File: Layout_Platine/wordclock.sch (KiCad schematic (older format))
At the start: 71 parts, among them IC1 ATmega8, P1 DCF_CONN_4, P10 CONN_1, P13 P_led, P14 CONN_2, P2 5V_CONN_2, P3 ISP, P4 UART_CONN_6, P5 Led_Zeilen_CONN_11, P6 Led_Spalten_CONN_11, P7 CONN_1, P8 CONN_1, P9 CONN_1, Q1 BC817, Q2 BC807, U1 LM317, U3 74HC04, X1 10MHz

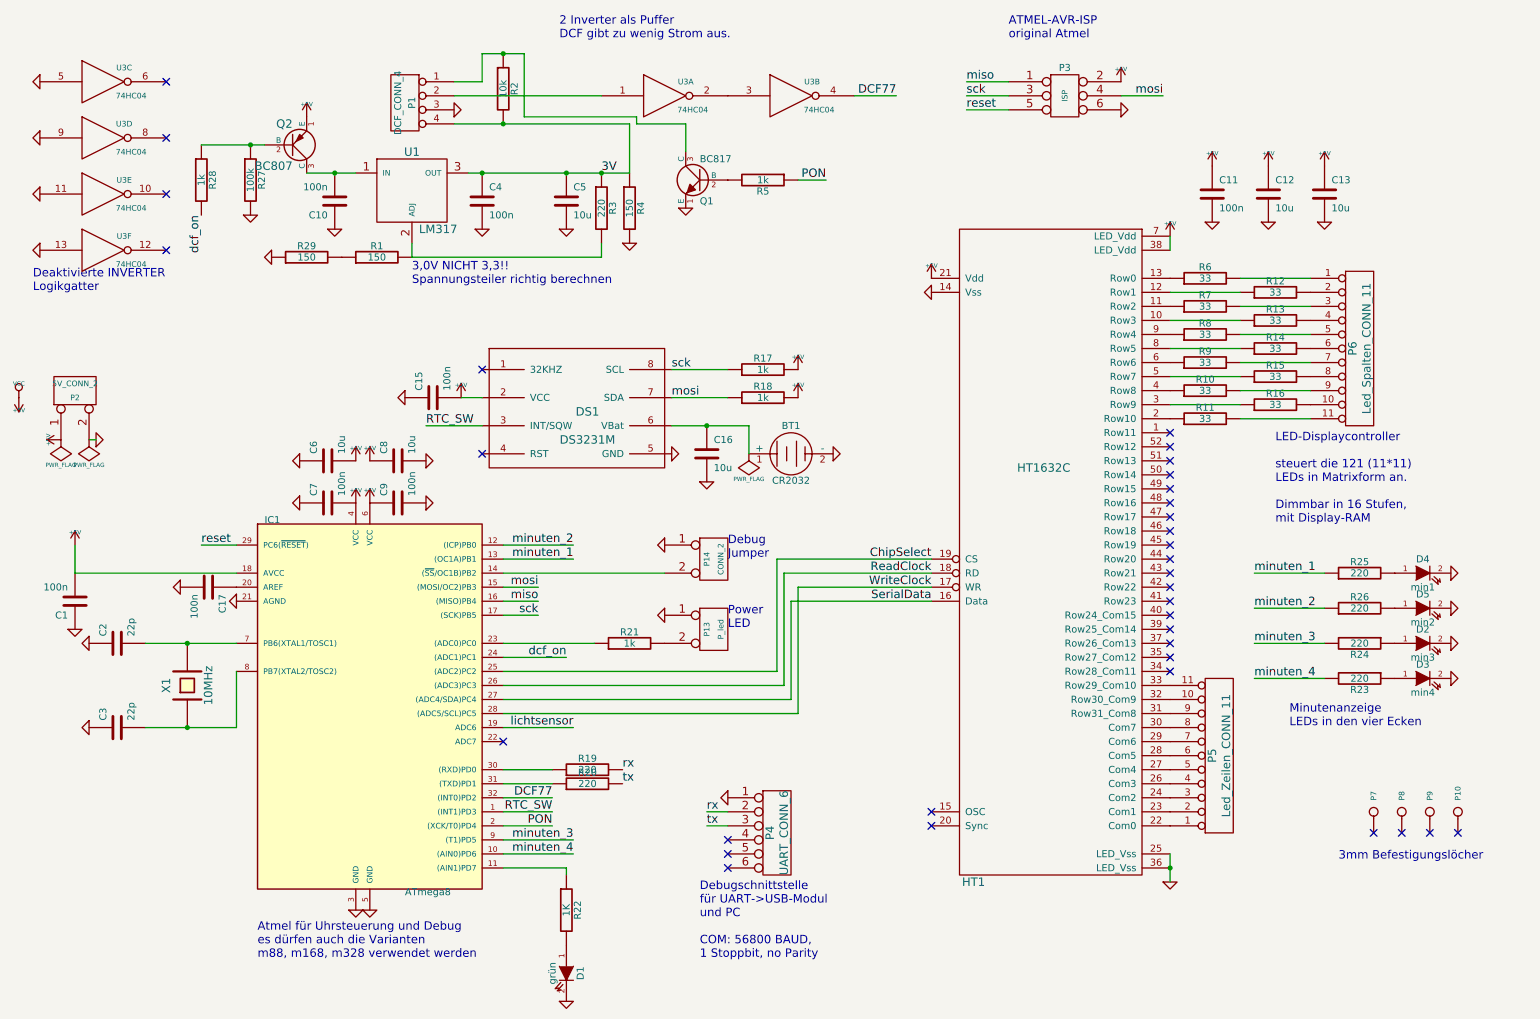
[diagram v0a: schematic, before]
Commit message: HardwareVersion 5 an sich fertig zur Herstellung. nur noch kleinere Änderungen, keine weiteren Features mehr.
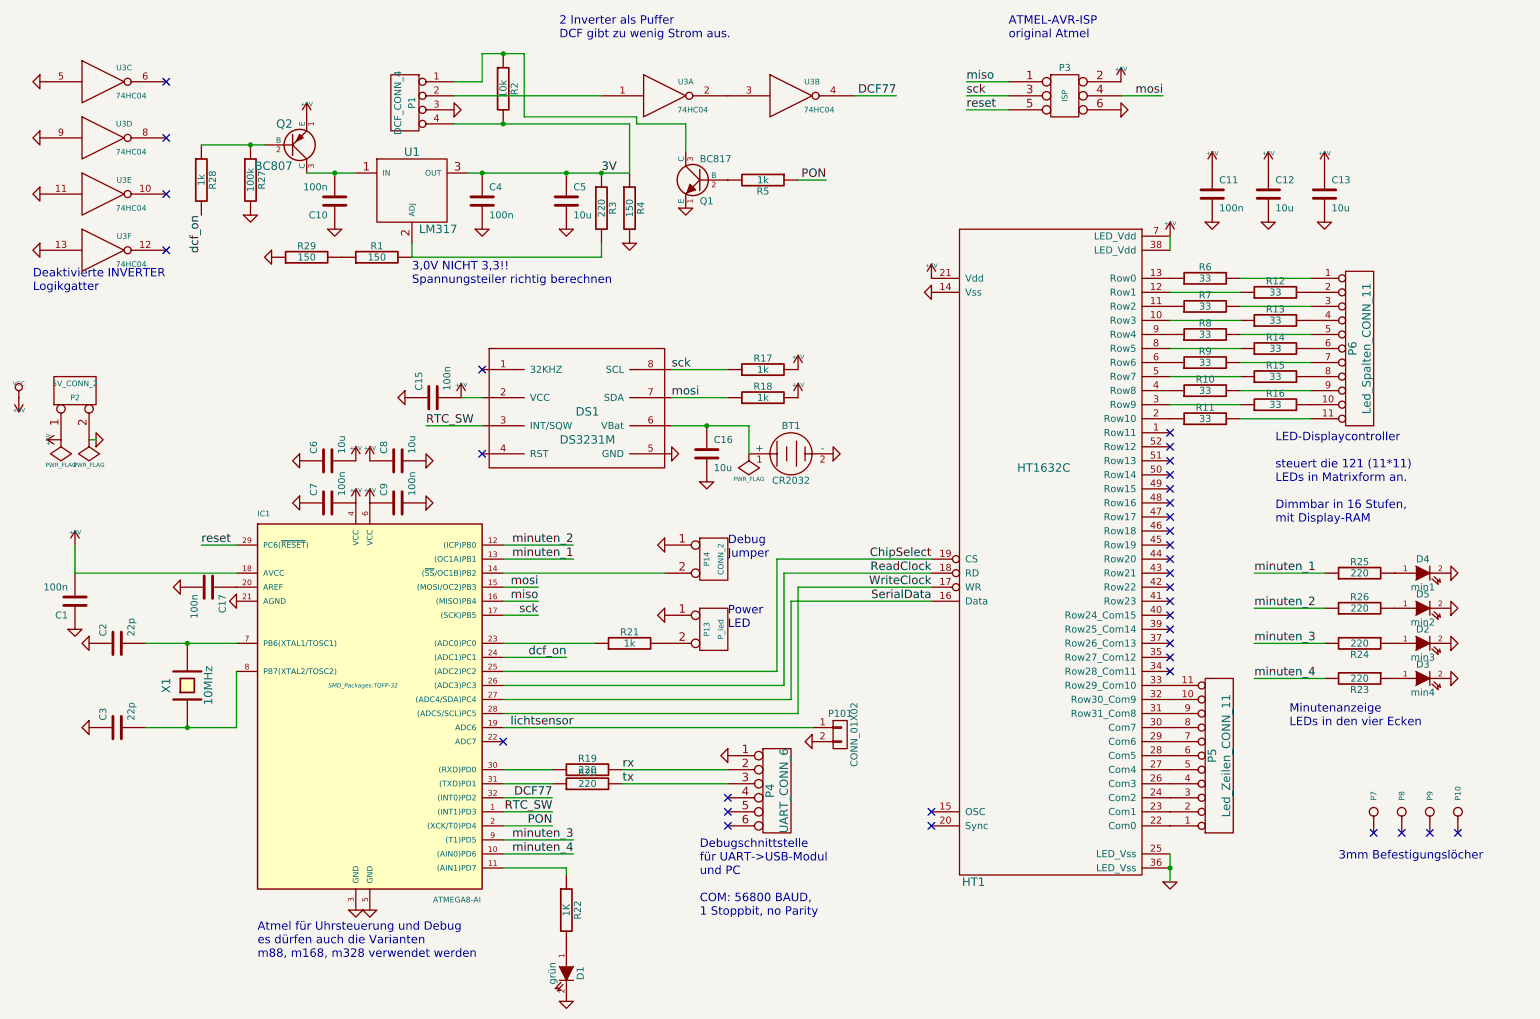
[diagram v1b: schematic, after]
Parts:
- added P101: CONN_01X02, Pin_Headers:Pin_Header_Straight_1x02, symbol CONN_01X02
- C12, C13, C16, C5, C8: footprint Capacitors_SMD:c_0805 -> Capacitors_SMD:C_0805
- IC1: value ATmega8 -> ATMEGA8-AI
- U3: footprint (none) -> SMD_Packages:SOIC-14_N
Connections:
- net GND: now also P101.2 (P2)
- net lichtsensor: now also P101.1 (P1)
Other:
- moved on the sheet: P4
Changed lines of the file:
@@
 EESchema Schematic File Version 2
-LIBS:atmega8-tq-ph
 LIBS:ht1632c
 LIBS:power
@@
 Connection ~ 3050 1750
 Wire Wire Line
-	2850 1750 3050 1750
-Wire Wire Line
-	3050 1750 3200 1750
+	2850 1750 3200 1750
 Connection ~ 2450 1550
 Wire Wire Line
-	2100 1550 2450 1550
-Wire Wire Line
-	2450 1550 2550 1550
+	2100 1550 2550 1550
 Wire Wire Line
 	9600 4600 10100 4600
@@
 Connection ~ 4700 1750
 Wire Wire Line
-	4000 1750 4100 1750
-Wire Wire Line
-	4100 1750 4700 1750
-Wire Wire Line
-	4700 1750 4950 1750
-Wire Wire Line
-	4950 1750 5150 1750
+	4000 1750 5150 1750
 Wire Wire Line
 	5850 3350 5450 3350
@@
 	6300 5500 6300 4800
 Wire Wire Line
-	4100 900  4250 900
-Wire Wire Line
-	4250 900  4400 900
+	4100 900  4400 900
 Wire Wire Line
 	4400 900  4400 1350
@@
 	4600 6200 4250 6200
 Wire Wire Line
-	5850 6300 5700 6300
+	5100 6000 5850 6000
 Wire Wire Line
 	7550 1200 7850 1200
@@
 	9000 2300 9000 2200
 Wire Wire Line
-	9000 6600 9000 6700
-Wire Wire Line
-	9000 6700 9000 6800
+	9000 6600 9000 6800
 Connection ~ 9000 6700
 Wire Wire Line
@@
 	1200 4600 2350 4600
 Wire Wire Line
-	1700 5100 2000 5100
-Wire Wire Line
-	2000 5100 2350 5100
+	1700 5100 2350 5100
 Connection ~ 2000 5100
 Wire Wire Line
-	1700 5700 2000 5700
-Wire Wire Line
-	2000 5700 2350 5700
+	1700 5700 2350 5700
 Connection ~ 2000 5700
 Wire Wire Line
@@
 	7550 1300 7850 1300
 Wire Wire Line
-	5700 6400 5850 6400
+	5100 6100 5850 6100
 Wire Wire Line
 	4250 6000 4600 6000
@@
 	3600 2350 3600 2250
 Wire Wire Line
-	3900 1400 4250 1400
-Wire Wire Line
-	4250 1400 5150 1400
+	3900 1400 5150 1400
 Wire Wire Line
 	5150 1400 5150 1750
@@
 	6000 3550 6000 3750
 Wire Wire Line
-	5450 3550 5700 3550
-Wire Wire Line
-	5700 3550 6000 3550
+	5450 3550 6000 3550
 Wire Wire Line
 	5400 4600 4250 4600
@@
 F 0 "C16" H 5750 3850 50  0000 L CNN
 F 1 "10u" H 5750 3650 50  0000 L CNN
-F 2 "Capacitors_SMD:c_0805" H 5700 3750 60  0001 C CNN
+F 2 "Capacitors_SMD:C_0805" H 5700 3750 60  0001 C CNN
 F 3 "" H 5700 3750 60  0001 C CNN
 	1    5700 3750
@@
 	1    0    0    -1
 $EndComp
-NoConn ~ 5850 6500
+NoConn ~ 5850 6200
 $Comp
 L PWR_FLAG #FLG011
@@
 Text Notes 3600 2550 0    60   ~ 0
 3,0V NICHT 3,3!!\nSpannungsteiler richtig berechnen
-Text Notes 5650 7350 0    60   ~ 0
+Text Notes 5650 7050 0    60   ~ 0
 Debugschnittstelle\nfür UART->USB-Modul\nund PC\n\nCOM: 56800 BAUD,\n1 Stoppbit, no Parity
 Text Notes 7850 800  0    60   ~ 0
@@
 F 0 "U3" H 1550 2400 40  0000 C CNN
 F 1 "74HC04" H 1600 2200 40  0000 C CNN
-F 2 "" H 1400 2300 60  0001 C CNN
+F 2 "SMD_Packages:SOIC-14_N" H 1400 2300 60  0001 C CNN
 F 3 "" H 1400 2300 60  0001 C CNN
 	6    1400 2300
@@
 F 0 "U3" H 1550 2000 40  0000 C CNN
 F 1 "74HC04" H 1600 1800 40  0000 C CNN
-F 2 "" H 1400 1900 60  0001 C CNN
+F 2 "SMD_Packages:SOIC-14_N" H 1400 1900 60  0001 C CNN
 F 3 "" H 1400 1900 60  0001 C CNN
 	5    1400 1900
@@
 F 0 "U3" H 1550 1600 40  0000 C CNN
 F 1 "74HC04" H 1600 1400 40  0000 C CNN
-F 2 "" H 1400 1500 60  0001 C CNN
+F 2 "SMD_Packages:SOIC-14_N" H 1400 1500 60  0001 C CNN
 F 3 "" H 1400 1500 60  0001 C CNN
 	4    1400 1500
@@
 F 0 "U3" H 1550 1200 40  0000 C CNN
 F 1 "74HC04" H 1600 1000 40  0000 C CNN
-F 2 "" H 1400 1100 60  0001 C CNN
+F 2 "SMD_Packages:SOIC-14_N" H 1400 1100 60  0001 C CNN
 F 3 "" H 1400 1100 60  0001 C CNN
 	3    1400 1100
@@
 F 0 "U3" H 6450 1300 40  0000 C CNN
 F 1 "74HC04" H 6500 1100 40  0000 C CNN
-F 2 "" H 6300 1200 60  0001 C CNN
+F 2 "SMD_Packages:SOIC-14_N" H 6300 1200 60  0001 C CNN
 F 3 "" H 6300 1200 60  0001 C CNN
 	2    6300 1200
@@
 F 0 "U3" H 5550 1300 40  0000 C CNN
 F 1 "74HC04" H 5600 1100 40  0000 C CNN
-F 2 "" H 5400 1200 60  0001 C CNN
+F 2 "SMD_Packages:SOIC-14_N" H 5400 1200 60  0001 C CNN
 F 3 "" H 5400 1200 60  0001 C CNN
 	1    5400 1200
@@
 Text Label 4600 6200 2    60   ~ 0
 DCF77
-NoConn ~ 5850 6700
-NoConn ~ 5850 6600
+NoConn ~ 5850 6400
+NoConn ~ 5850 6300
 $Comp
 L GND #PWR044
 U 1 1 4F80AAE2
-P 5850 6200
-F 0 "#PWR044" H 5850 6200 30  0001 C CNN
-F 1 "GND" H 5850 6130 30  0001 C CNN
-F 2 "" H 5850 6200 60  0001 C CNN
-F 3 "" H 5850 6200 60  0001 C CNN
-	1    5850 6200
-	0    1    1    0
-$EndComp
-Text Label 5700 6400 0    60   ~ 0
-tx
+P 5850 5900
+F 0 "#PWR044" H 5850 5900 30  0001 C CNN
+F 1 "GND" H 5850 5830 30  0001 C CNN
+F 2 "" H 5850 5900 60  0001 C CNN
+F 3 "" H 5850 5900 60  0001 C CNN
+	1    5850 5900
+	0    1    1    0
+$EndComp
 Text Label 5100 6100 0    60   ~ 0
 tx
 Text Label 5100 6000 0    60   ~ 0
 rx
-Text Label 5700 6300 0    60   ~ 0
-rx
 $Comp
 L CONN_6 P4
 U 1 1 4F80A9BA
-P 6200 6450
-F 0 "P4" V 6150 6450 60  0000 C CNN
-F 1 "UART_CONN_6" V 6250 6450 60  0000 C CNN
-F 2 "Pin_Headers:Pin_Header_Angled_1x06" H 6200 6450 60  0001 C CNN
-F 3 "" H 6200 6450 60  0001 C CNN
-	1    6200 6450
+P 6200 6150
+F 0 "P4" V 6150 6150 60  0000 C CNN
+F 1 "UART_CONN_6" V 6250 6150 60  0000 C CNN
+F 2 "Pin_Headers:Pin_Header_Angled_1x06" H 6200 6150 60  0001 C CNN
+F 3 "" H 6200 6150 60  0001 C CNN
+	1    6200 6150
 	1    0    0    -1
 $EndComp
@@
 	1    2000 5400
 	0    -1   -1   0
-$EndComp
-$Comp
-L ATMEGA8-AI IC1
-U 1 1 4F80A6A4
-P 3250 5400
-F 0 "IC1" H 2550 6550 50  0000 L BNN
-F 1 "ATmega8" H 3550 3900 50  0000 L BNN
-F 2 "SMD_Packages:TQFP-32" H 2700 3950 50  0001 C CNN
-F 3 "" H 3250 5400 60  0001 C CNN
-	1    3250 5400
-	1    0    0    -1
 $EndComp
 $Comp
@@
 F 0 "C13" H 10150 2000 50  0000 L CNN
 F 1 "10u" H 10150 1800 50  0000 L CNN
-F 2 "Capacitors_SMD:c_0805" H 10100 1900 60  0001 C CNN
+F 2 "Capacitors_SMD:C_0805" H 10100 1900 60  0001 C CNN
 F 3 "" H 10100 1900 60  0001 C CNN
 	1    10100 1900
@@
 F 0 "C12" H 9750 2000 50  0000 L CNN
 F 1 "10u" H 9750 1800 50  0000 L CNN
-F 2 "Capacitors_SMD:c_0805" H 9700 1900 60  0001 C CNN
+F 2 "Capacitors_SMD:C_0805" H 9700 1900 60  0001 C CNN
 F 3 "" H 9700 1900 60  0001 C CNN
 	1    9700 1900
@@
 F 0 "C8" H 3550 3900 50  0000 L CNN
 F 1 "10u" H 3550 3700 50  0000 L CNN
-F 2 "Capacitors_SMD:c_0805" H 3500 3800 60  0001 C CNN
+F 2 "Capacitors_SMD:C_0805" H 3500 3800 60  0001 C CNN
 F 3 "" H 3500 3800 60  0001 C CNN
 	1    3500 3800
@@
 F 0 "C5" H 4750 2050 50  0000 L CNN
 F 1 "10u" H 4750 1850 50  0000 L CNN
-F 2 "Capacitors_SMD:c_0805" H 4700 1950 60  0001 C CNN
+F 2 "Capacitors_SMD:C_0805" H 4700 1950 60  0001 C CNN
 F 3 "" H 4700 1950 60  0001 C CNN
 	1    4700 1950
@@
 Minutenanzeige\nLEDs in den vier Ecken
 Wire Wire Line
-	4250 5700 4750 5700
+	4250 5700 6450 5700
 Text Label 4750 5700 2    60   ~ 0
 lichtsensor
+$Comp
+L ATMEGA8-AI IC1
+U 1 1 5415DF5B
+P 3250 5400
+F 0 "IC1" H 2500 6600 40  0000 L BNN
+F 1 "ATMEGA8-AI" H 3750 3850 40  0000 L BNN
+F 2 "SMD_Packages:TQFP-32" H 3250 5400 30  0000 C CIN
+F 3 "" H 3250 5400 60  0000 C CNN
+	1    3250 5400
+	1    0    0    -1
+$EndComp
+$Comp
+L CONN_01X02 P101
+U 1 1 543227B9
+P 6650 5750
+F 0 "P101" H 6650 5900 50  0000 C CNN
+F 1 "CONN_01X02" V 6750 5750 50  0000 C CNN
+F 2 "Pin_Headers:Pin_Header_Straight_1x02" H 6650 5750 60  0001 C CNN
+F 3 "" H 6650 5750 60  0000 C CNN
+	1    6650 5750
+	1    0    0    -1
+$EndComp
+$Comp
+L GND #PWR064
+U 1 1 5432292C
+P 6450 5800
+F 0 "#PWR064" H 6450 5800 30  0001 C CNN
+F 1 "GND" H 6450 5730 30  0001 C CNN
+F 2 "" H 6450 5800 60  0001 C CNN
+F 3 "" H 6450 5800 60  0001 C CNN
+	1    6450 5800
+	0    1    1    0
+$EndComp
 $EndSCHEMATC

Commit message: Minuten-LEDs jetzt mit Durchkontaktierung für bessere mechanische Stabilität.
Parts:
- C12, C13, C16, C5, C8: footprint Capacitors_SMD:C_0805 -> SMD_Packages:SMD-0805
- C6: footprint Capacitors_SMD:c_0805 -> SMD_Packages:SMD-0805
- D2, D3, D4, D5: footprint Connect:GS2 -> Pin_Headers:Pin_Header_Straight_1x02
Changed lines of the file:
@@
 F 0 "C16" H 5750 3850 50  0000 L CNN
 F 1 "10u" H 5750 3650 50  0000 L CNN
-F 2 "Capacitors_SMD:C_0805" H 5700 3750 60  0001 C CNN
+F 2 "SMD_Packages:SMD-0805" H 5700 3750 60  0001 C CNN
 F 3 "" H 5700 3750 60  0001 C CNN
 	1    5700 3750
@@
 F 0 "D2" H 10800 5200 50  0000 C CNN
 F 1 "min3" H 10800 5000 50  0000 C CNN
-F 2 "Connect:GS2" H 10800 5100 60  0001 C CNN
+F 2 "Pin_Headers:Pin_Header_Straight_1x02" H 10800 5100 60  0001 C CNN
 F 3 "" H 10800 5100 60  0001 C CNN
 	1    10800 5100
@@
 F 0 "D3" H 10800 5450 50  0000 C CNN
 F 1 "min4" H 10800 5250 50  0000 C CNN
-F 2 "Connect:GS2" H 10800 5350 60  0001 C CNN
+F 2 "Pin_Headers:Pin_Header_Straight_1x02" H 10800 5350 60  0001 C CNN
 F 3 "" H 10800 5350 60  0001 C CNN
 	1    10800 5350
@@
 F 0 "D4" H 10800 4700 50  0000 C CNN
 F 1 "min1" H 10800 4500 50  0000 C CNN
-F 2 "Connect:GS2" H 10800 4600 60  0001 C CNN
+F 2 "Pin_Headers:Pin_Header_Straight_1x02" H 10800 4600 60  0001 C CNN
 F 3 "" H 10800 4600 60  0001 C CNN
 	1    10800 4600
@@
 F 0 "D5" H 10800 4950 50  0000 C CNN
 F 1 "min2" H 10800 4750 50  0000 C CNN
-F 2 "Connect:GS2" H 10800 4850 60  0001 C CNN
+F 2 "Pin_Headers:Pin_Header_Straight_1x02" H 10800 4850 60  0001 C CNN
 F 3 "" H 10800 4850 60  0001 C CNN
 	1    10800 4850
@@
 F 0 "C13" H 10150 2000 50  0000 L CNN
 F 1 "10u" H 10150 1800 50  0000 L CNN
-F 2 "Capacitors_SMD:C_0805" H 10100 1900 60  0001 C CNN
+F 2 "SMD_Packages:SMD-0805" H 10100 1900 60  0001 C CNN
 F 3 "" H 10100 1900 60  0001 C CNN
 	1    10100 1900
@@
 F 0 "C12" H 9750 2000 50  0000 L CNN
 F 1 "10u" H 9750 1800 50  0000 L CNN
-F 2 "Capacitors_SMD:C_0805" H 9700 1900 60  0001 C CNN
+F 2 "SMD_Packages:SMD-0805" H 9700 1900 60  0001 C CNN
 F 3 "" H 9700 1900 60  0001 C CNN
 	1    9700 1900
@@
 F 0 "C6" H 3050 3900 50  0000 L CNN
 F 1 "10u" H 3050 3700 50  0000 L CNN
-F 2 "Capacitors_SMD:c_0805" H 3000 3800 60  0001 C CNN
+F 2 "SMD_Packages:SMD-0805" H 3000 3800 60  0001 C CNN
 F 3 "" H 3000 3800 60  0001 C CNN
 	1    3000 3800
@@
 F 0 "C8" H 3550 3900 50  0000 L CNN
 F 1 "10u" H 3550 3700 50  0000 L CNN
-F 2 "Capacitors_SMD:C_0805" H 3500 3800 60  0001 C CNN
+F 2 "SMD_Packages:SMD-0805" H 3500 3800 60  0001 C CNN
 F 3 "" H 3500 3800 60  0001 C CNN
 	1    3500 3800
@@
 F 0 "C5" H 4750 2050 50  0000 L CNN
 F 1 "10u" H 4750 1850 50  0000 L CNN
-F 2 "Capacitors_SMD:C_0805" H 4700 1950 60  0001 C CNN
+F 2 "SMD_Packages:SMD-0805" H 4700 1950 60  0001 C CNN
 F 3 "" H 4700 1950 60  0001 C CNN
 	1    4700 1950
